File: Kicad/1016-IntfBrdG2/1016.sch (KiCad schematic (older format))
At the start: 10 parts, among them P1 TST, P2 CONN_4, P3 CONN_4, P4 CONN_4, P5 CONN_4X2, P6 CONN_4X2, P7 CONN_4

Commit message: Updates to silkscreen and created mashup.  These Gerbers sent to PCB house.
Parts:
- R1: value 100K -> 0
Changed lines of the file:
@@
 Sheet 1 1
 Title "Interface Board (Gen 2)"
-Date "27 jul 2015"
+Date "28 jul 2015"
 Rev "-"
 Comp "Open Pinball Project"
@@
 P 2950 4700
 F 0 "R1" V 3030 4700 40  0000 C CNN
-F 1 "100K" V 2957 4701 40  0000 C CNN
+F 1 "0" V 2957 4701 40  0000 C CNN
 F 2 "~" V 2880 4700 30  0000 C CNN
 F 3 "~" H 2950 4700 30  0000 C CNN

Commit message: Gen2 embedded code: Remove debug code that always overwrites NV configuration.  Added Gen2.rev0.1.1.0.cyacd for downloading to boards.
PopulateBrd document:
Correct solenoid pinout picture.

SolDrvG2 board:
Move location of 4 pin switch input header to reduce interference with interface board.  Update to use cheaper 6 pin Molex header.  Add rev to copper layer.

IntfBrdG2 board:
Change future pin on ribbon cable connector to carry 12V.  Make board slightly larger so it can be panellized by IteadStudio.  Add better grounding.  Move ribbon cable connectors so less interference with solenoid board input header.  Add 3 pin header to make communicating with first board in chain easier (switch comms between 4 pin header and ribbon cable).  Add rev to copper layer.

IncandSMG2 board:
Update to use cheaper 2 pin Molex header.  Add rev to copper layer.

Panellize Gerbers:
Add panellized boards for SolDrvG2, IntfBrdG2, and IncandSMG2.

MPF/SS3:
Small updates to add skillshot.
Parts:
- added P15: CONN_2, symbol CONN_2
- added P8: CONN_3, symbol CONN_3
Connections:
- net labels removed: FUTURE, P3
- wire segments 73 -> 78
- no-connect marks 5 -> 6
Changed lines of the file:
@@
 Sheet 1 1
 Title "Interface Board (Gen 2)"
-Date "28 jul 2015"
-Rev "-"
+Date "8 apr 2016"
+Rev "1"
 Comp "Open Pinball Project"
 Comment1 ""
@@
 	2600 3300 2600 4400
 Wire Wire Line
-	2600 3600 2900 3600
+	2100 3600 2900 3600
 Wire Wire Line
 	2900 3600 2900 3400
@@
 Text Label 4650 4300 0    60   ~ 0
 P2
-Text Label 4650 4200 0    60   ~ 0
-P3
 $Comp
 L CONN_4 P4
@@
 	5800 4300 5800 6200
 Wire Wire Line
-	6600 4500 6600 4700
-Wire Wire Line
-	6600 4700 5900 4700
-Wire Wire Line
-	5900 4200 5900 6100
-Wire Wire Line
-	5900 4200 4600 4200
+	6600 4700 6600 4500
+Wire Wire Line
+	5500 4700 6600 4700
 Wire Wire Line
 	5900 6100 6600 6100
@@
 Text Label 4950 4300 0    60   ~ 0
 SYNCH
-Text Label 4950 4200 0    60   ~ 0
-FUTURE
 $Comp
 L R R3
@@
 Connection ~ 6300 4600
 Wire Wire Line
-	7300 4900 7300 4400
-Wire Wire Line
-	7300 4400 7700 4400
+	7300 4900 7300 3700
 Connection ~ 6800 4900
-Wire Wire Line
-	7500 3400 7500 4500
 Wire Wire Line
 	7500 4500 7700 4500
 Connection ~ 6800 3400
+$Comp
+L CONN_3 P8
+U 1 1 56FD1895
+P 8050 3800
+F 0 "P8" V 8000 3800 50  0000 C CNN
+F 1 "CONN_3" V 8100 3800 40  0000 C CNN
+F 2 "" H 8050 3800 60  0000 C CNN
+F 3 "" H 8050 3800 60  0000 C CNN
+	1    8050 3800
+	1    0    0    -1
+$EndComp
+Wire Wire Line
+	7100 3900 7700 3900
+Connection ~ 7100 3900
+Wire Wire Line
+	7500 3400 7500 4500
+Wire Wire Line
+	7300 3700 7700 3700
+Wire Wire Line
+	7700 3800 7600 3800
+Wire Wire Line
+	7600 3800 7600 4400
+Wire Wire Line
+	7600 4400 7700 4400
+$Comp
+L CONN_2 P15
+U 1 1 570704B2
+P 1750 3700
+F 0 "P15" V 1700 3700 40  0000 C CNN
+F 1 "CONN_2" V 1800 3700 40  0000 C CNN
+F 2 "" H 1750 3700 60  0000 C CNN
+F 3 "" H 1750 3700 60  0000 C CNN
+	1    1750 3700
+	-1   0    0    1
+$EndComp
+Wire Wire Line
+	2200 3600 2200 3800
+Wire Wire Line
+	2200 3800 2100 3800
+Connection ~ 2200 3600
+$Comp
+L +12V1 #PWR?
+U 1 1 570708B1
+P 5500 4700
+F 0 "#PWR?" H 5500 4650 20  0001 C CNN
+F 1 "+12V1" H 5500 4800 30  0000 C CNN
+F 2 "~" H 5500 4700 60  0000 C CNN
+F 3 "~" H 5500 4700 60  0000 C CNN
+	1    5500 4700
+	1    0    0    -1
+$EndComp
+Wire Wire Line
+	5900 4700 5900 6100
+NoConn ~ 4600 4200
 $EndSCHEMATC

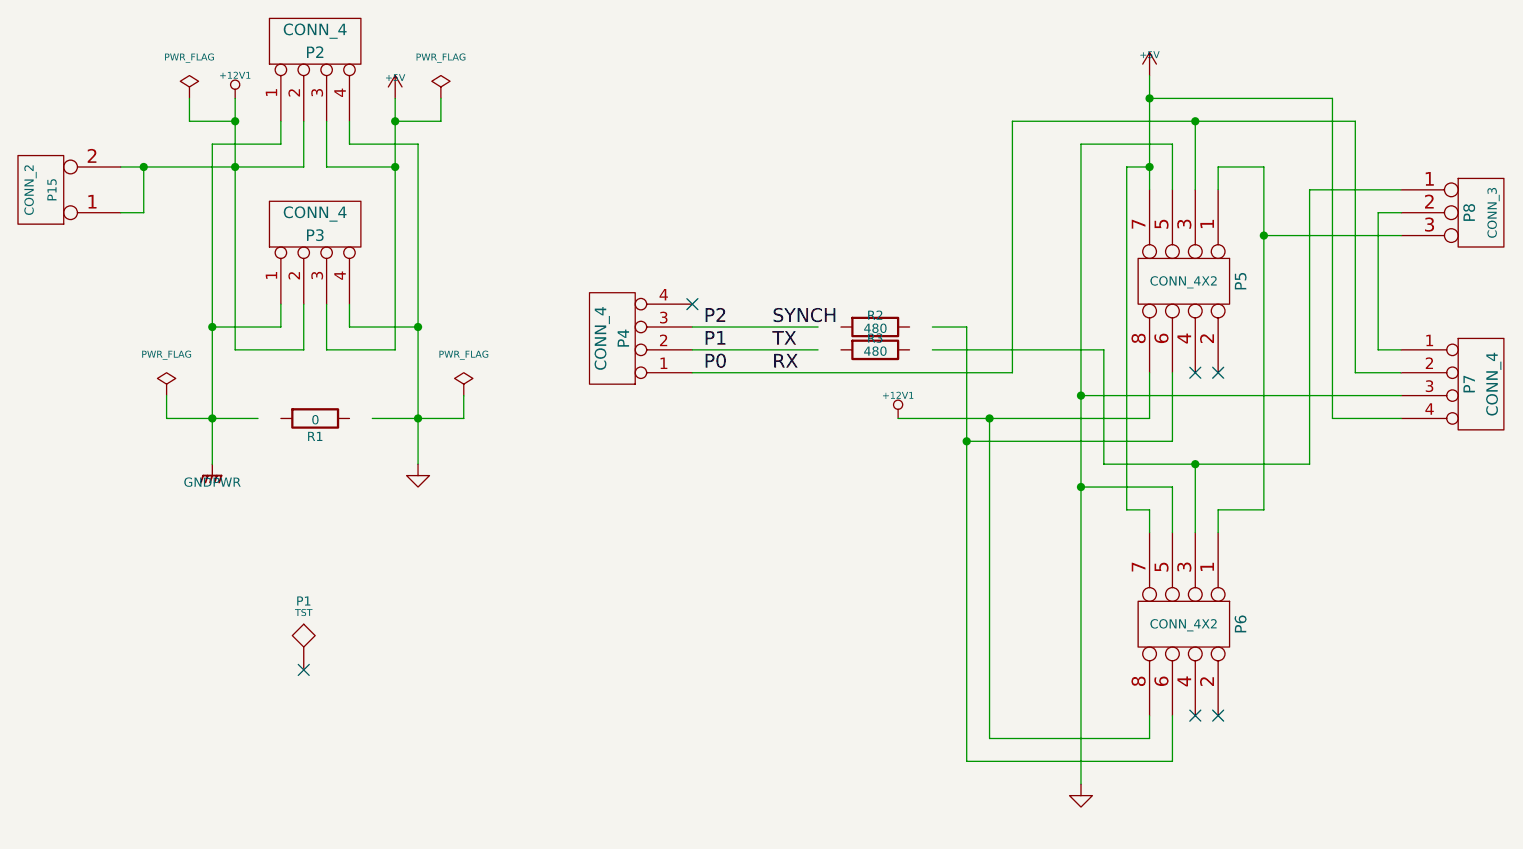
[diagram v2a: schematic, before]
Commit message: Rename 1012-InpSolGen2 to 1012-STM32F0InpSol to indicate it is for the STM32F0 Discovery board.  1012 is an untested and orphaned set of boards.  Rename 1015-InpBrdG2 to 1015-SpiNeoPxl.  1015 basically has a single pin used for connecting to Neopixels using the SPI bus.  Newer version uses the internal FPGA of the PSOC 4200 and uses a different output pin.  1015 is tested, but mostly orphaned since the FPGA version uses less memory and processing.
Update 1013-SolDrvG2, 1014-IncandBrdG2, and 1016-IntfBrdG2 to version 4.0.7 of KiCad.  Required updating the gnd and resistor symbols to match the new standard libraries.
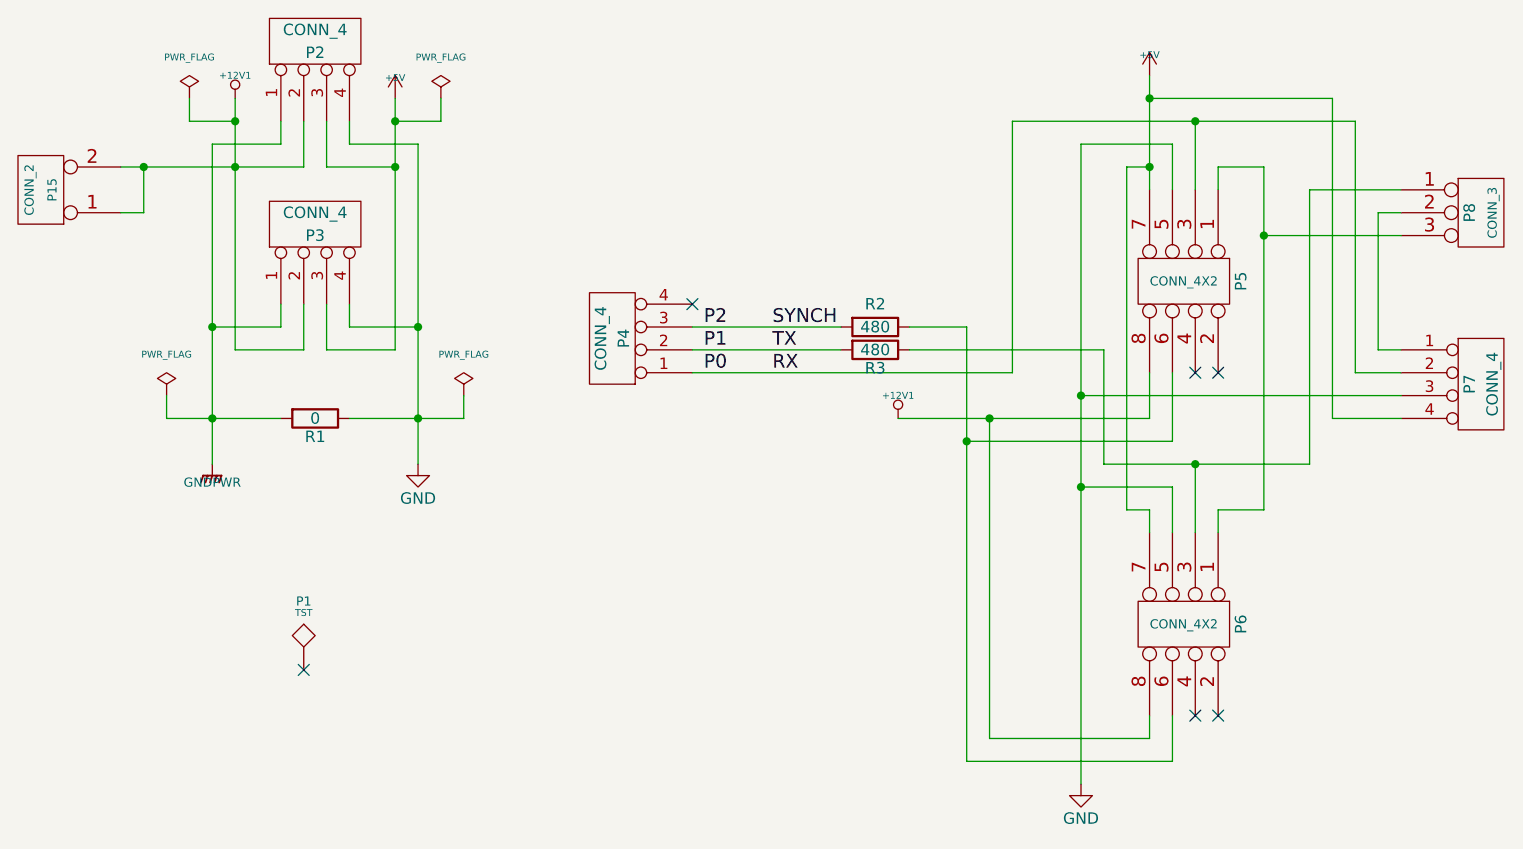
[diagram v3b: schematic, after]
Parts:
- R1, R2, R3: footprint ~ -> (none)
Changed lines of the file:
@@
 EESchema Schematic File Version 2
+LIBS:1016-rescue
 LIBS:commonpart
 LIBS:power
@@
 LIBS:memory
 LIBS:xilinx
-LIBS:special
 LIBS:microcontrollers
 LIBS:dsp
@@
 LIBS:valves
 LIBS:1016-cache
-EELAYER 27 0
+EELAYER 25 0
 EELAYER END
 $Descr A 11000 8500
@@
 $EndComp
 $Comp
-L GND #PWR03
-U 1 1 55B16408
-P 3400 4900
-F 0 "#PWR03" H 3400 4900 30  0001 C CNN
-F 1 "GND" H 3400 4830 30  0001 C CNN
-F 2 "" H 3400 4900 60  0001 C CNN
-F 3 "" H 3400 4900 60  0001 C CNN
-	1    3400 4900
-	1    0    0    -1
-$EndComp
-$Comp
 L +12V1 #PWR04
 U 1 1 55B165D8
@@
 	2800 4300 2500 4300
 Connection ~ 2500 4300
-$Comp
-L R R1
-U 1 1 55B1880D
-P 2950 4700
-F 0 "R1" V 3030 4700 40  0000 C CNN
-F 1 "0" V 2957 4701 40  0000 C CNN
-F 2 "~" V 2880 4700 30  0000 C CNN
-F 3 "~" H 2950 4700 30  0000 C CNN
-	1    2950 4700
-	0    1    1    0
-$EndComp
-Wire Wire Line
-	2300 4700 2700 4700
+Wire Wire Line
+	2300 4700 2800 4700
 Connection ~ 2500 4700
 Wire Wire Line
-	3200 4700 3600 4700
+	3100 4700 3600 4700
 Connection ~ 3400 4700
 $Comp
@@
 NoConn ~ 6800 6000
 NoConn ~ 6900 6000
-$Comp
-L GND #PWR09
-U 1 1 55B57D46
-P 6300 6300
-F 0 "#PWR09" H 6300 6300 30  0001 C CNN
-F 1 "GND" H 6300 6230 30  0001 C CNN
-F 2 "" H 6300 6300 60  0001 C CNN
-F 3 "" H 6300 6300 60  0001 C CNN
-	1    6300 6300
-	1    0    0    -1
-$EndComp
 Wire Wire Line
 	6700 3700 6700 3500
@@
 Text Label 4950 4300 0    60   ~ 0
 SYNCH
-$Comp
-L R R3
-U 1 1 55B57FF4
-P 5400 4400
-F 0 "R3" V 5350 4400 40  0000 C CNN
-F 1 "480" V 5407 4401 40  0000 C CNN
-F 2 "~" V 5330 4400 30  0000 C CNN
-F 3 "~" H 5400 4400 30  0000 C CNN
-	1    5400 4400
-	0    1    1    0
-$EndComp
-Wire Wire Line
-	4600 4400 5150 4400
-Wire Wire Line
-	5650 4400 6400 4400
-$Comp
-L R R2
-U 1 1 55B58106
-P 5400 4300
-F 0 "R2" V 5350 4300 40  0000 C CNN
-F 1 "480" V 5407 4301 40  0000 C CNN
-F 2 "~" V 5330 4300 30  0000 C CNN
-F 3 "~" H 5400 4300 30  0000 C CNN
-	1    5400 4300
-	0    1    1    0
-$EndComp
-Wire Wire Line
-	4600 4300 5150 4300
-Wire Wire Line
-	5650 4300 5800 4300
+Wire Wire Line
+	4600 4400 5250 4400
+Wire Wire Line
+	5550 4400 6400 4400
+Wire Wire Line
+	4600 4300 5250 4300
+Wire Wire Line
+	5550 4300 5800 4300
 $Comp
 L CONN_4 P7
@@
 	5900 4700 5900 6100
 NoConn ~ 4600 4200
+$Comp
+L R R1
+U 1 1 5A54E8FB
+P 2950 4700
+F 0 "R1" V 3030 4700 50  0000 C CNN
+F 1 "0" V 2950 4700 50  0000 C CNN
+F 2 "" V 2880 4700 50  0001 C CNN
+F 3 "" H 2950 4700 50  0001 C CNN
+	1    2950 4700
+	0    1    1    0
+$EndComp
+$Comp
+L GND #PWR?
+U 1 1 5A54E968
+P 6300 6300
+F 0 "#PWR?" H 6300 6050 50  0001 C CNN
+F 1 "GND" H 6300 6150 50  0000 C CNN
+F 2 "" H 6300 6300 50  0001 C CNN
+F 3 "" H 6300 6300 50  0001 C CNN
+	1    6300 6300
+	1    0    0    -1
+$EndComp
+$Comp
+L GND #PWR?
+U 1 1 5A54EAD5
+P 3400 4900
+F 0 "#PWR?" H 3400 4650 50  0001 C CNN
+F 1 "GND" H 3400 4750 50  0000 C CNN
+F 2 "" H 3400 4900 50  0001 C CNN
+F 3 "" H 3400 4900 50  0001 C CNN
+	1    3400 4900
+	1    0    0    -1
+$EndComp
+$Comp
+L R R2
+U 1 1 5A54EC62
+P 5400 4300
+F 0 "R2" V 5300 4300 50  0000 C CNN
+F 1 "480" V 5400 4300 50  0000 C CNN
+F 2 "" V 5330 4300 50  0001 C CNN
+F 3 "" H 5400 4300 50  0001 C CNN
+	1    5400 4300
+	0    1    1    0
+$EndComp
+$Comp
+L R R3
+U 1 1 5A54F0BB
+P 5400 4400
+F 0 "R3" V 5480 4400 50  0000 C CNN
+F 1 "480" V 5400 4400 50  0000 C CNN
+F 2 "" V 5330 4400 50  0001 C CNN
+F 3 "" H 5400 4400 50  0001 C CNN
+	1    5400 4400
+	0    1    1    0
+$EndComp
 $EndSCHEMATC
